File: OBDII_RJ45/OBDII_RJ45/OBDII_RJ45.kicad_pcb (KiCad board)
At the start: 2 copper layers, 19.7 x 22.2 mm, 2 parts, among them J1 Cantact, J2 Conn_01x02

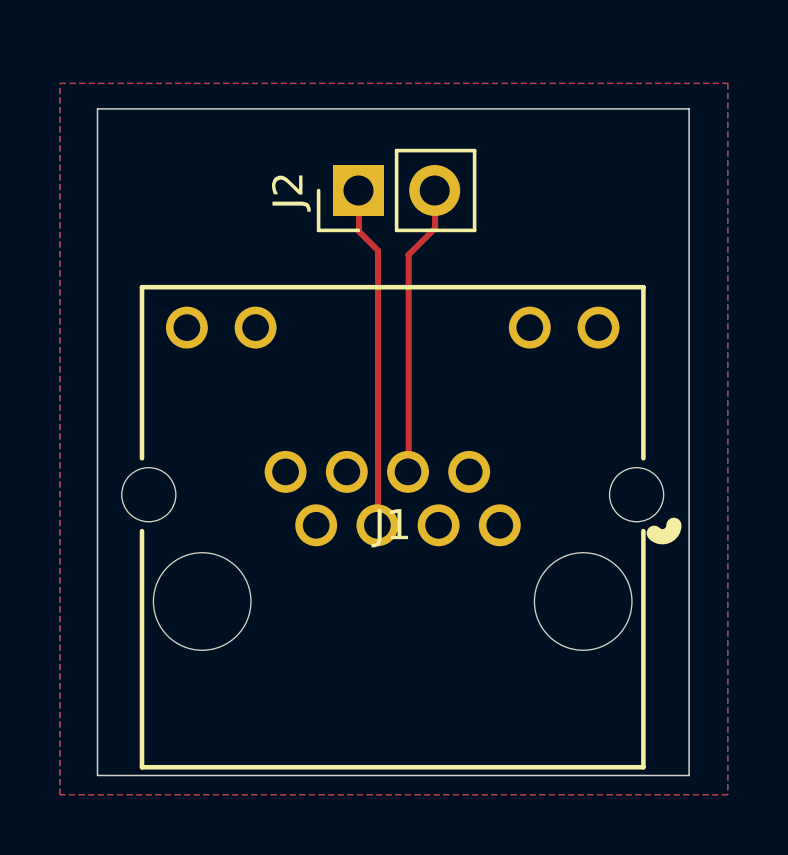
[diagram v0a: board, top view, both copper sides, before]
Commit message: feat: add GND between OBDII connector & OBDII_RJ45
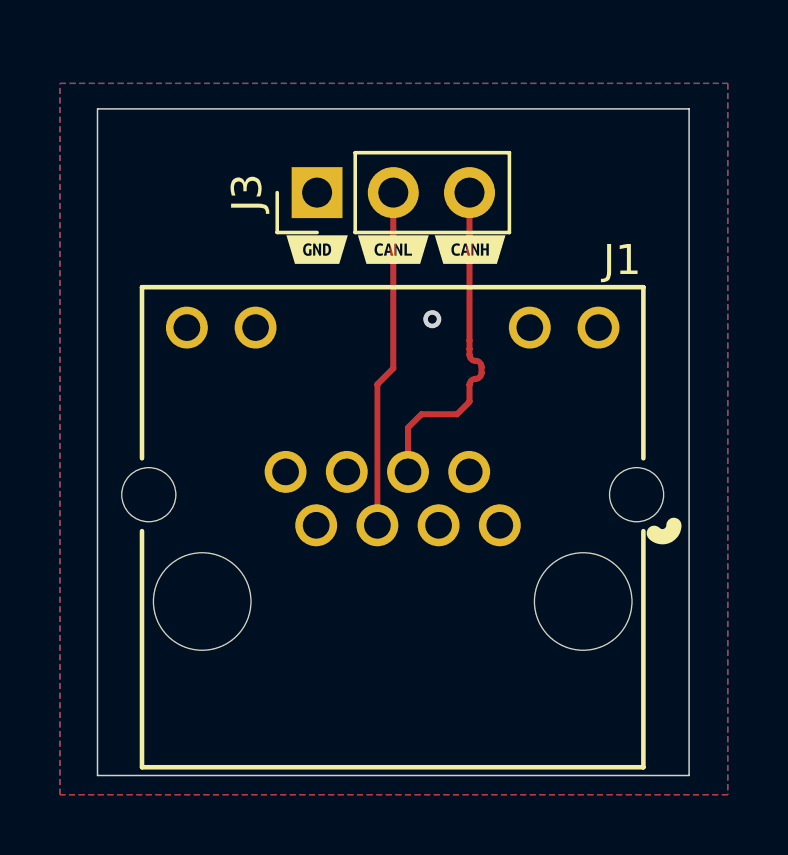
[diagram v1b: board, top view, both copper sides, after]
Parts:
- removed J2: Conn_01x02, Connector_PinHeader_2.54mm:PinHeader_1x02_P2.54mm_Vertical
- added J3: Conn_01x03, Connector_PinHeader_2.54mm:PinHeader_1x03_P2.54mm_Vertical, F.Cu at (22.3, 17.8)
- added kibuzzard-67DDB05E: G***, kibuzzard-67DDB05E, F.Cu at (27.4, 19.7)
- added kibuzzard-67DDB066: G***, kibuzzard-67DDB066, F.Cu at (24.9, 19.7)
- added kibuzzard-67DDB06D: G***, kibuzzard-67DDB06D, F.Cu at (22.3, 19.7)
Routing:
- net /CANH: track 9.76 -> 11.3 mm
- net GND: vias 0 -> 1

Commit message: feat(hw): add lcsc parts
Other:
- board size 19.7 x 22.2 mm -> 19.7 x 23.4 mm
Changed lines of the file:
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@@
 				(font
 					(size 0.001 0.001)
+					(thickness 0.15)
 				)
 			)
@@
 				(font
 					(size 0.001 0.001)
+					(thickness 0.15)
 				)
 			)
@@
 				(font
 					(size 0.001 0.001)
+					(thickness 0.15)
 				)
 			)
@@
 				(font
 					(size 0.001 0.001)
+					(thickness 0.15)
 				)
 			)
@@
 				(font
 					(size 0.001 0.001)
+					(thickness 0.15)
 				)
 			)
@@
 				(font
 					(size 0.001 0.001)
+					(thickness 0.15)
 				)
 			)
@@
 	)
 	(gr_rect
-		(start 15 15)
+		(start 15 13.79)
 		(end 34.72 37.22)
 		(stroke
@@
 		(polygon
 			(pts
-				(xy 13.75 14.15) (xy 36.01 14.15) (xy 36.01 37.86) (xy 13.75 37.86)
-			)
-		)
+				(xy 13.75 13.37) (xy 36.01 13.37) (xy 36.01 37.86) (xy 13.75 37.86)
+			)
+		)

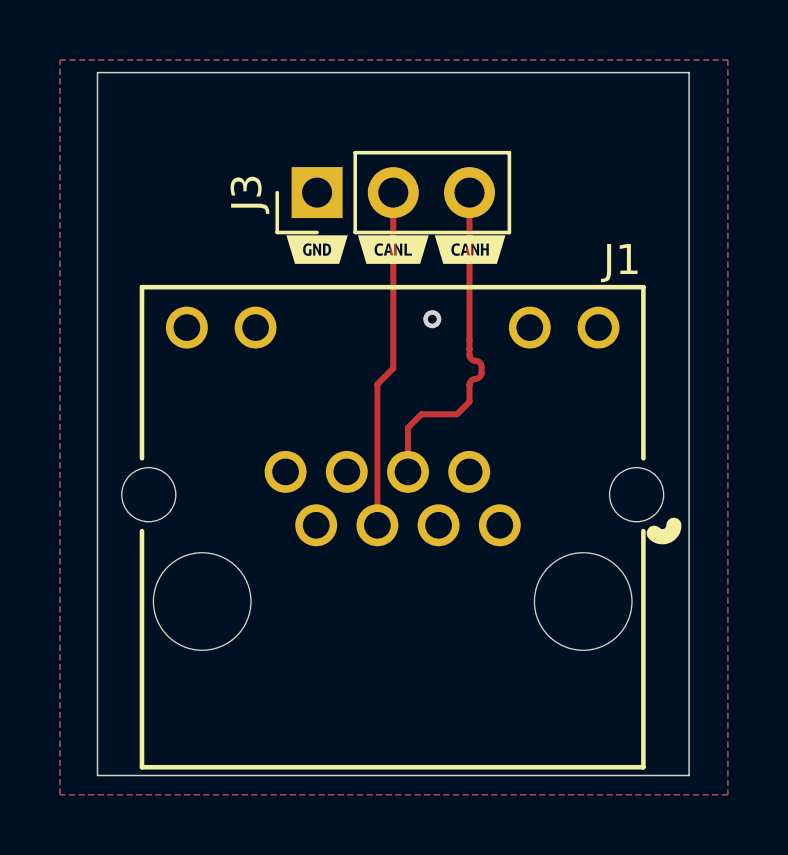
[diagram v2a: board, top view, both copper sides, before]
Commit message: feat(Hw):Update_Labels
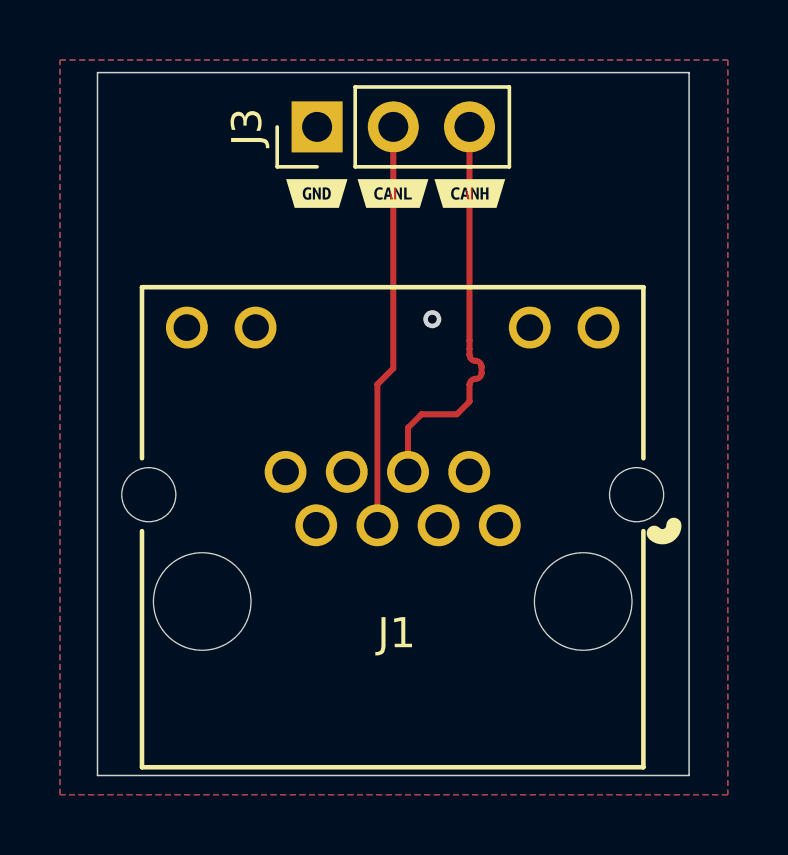
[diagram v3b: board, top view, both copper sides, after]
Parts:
- added G***: LOGO, Aesthetics:electronic_cats_logo_4x3, B.Cu at (24.9, 22.7)
- added kibuzzard-67FE8E6B: G***, kibuzzard-67FE8E6B, B.Cu at (24.9, 34.3)
- moved J3 2.19 mm to (22.3, 15.6)
- moved kibuzzard-67DDB05E 1.87 mm to (27.4, 17.8)
- moved kibuzzard-67DDB06D 1.87 mm to (22.3, 17.8)
- moved kibuzzard-67DDB066 1.87 mm to (24.9, 17.8)
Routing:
- net /CANH: track 11.3 -> 13.5 mm
- net /CANL: track 11.3 -> 13.5 mm

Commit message: Fix: CANbus routing for OBDII_RJ45
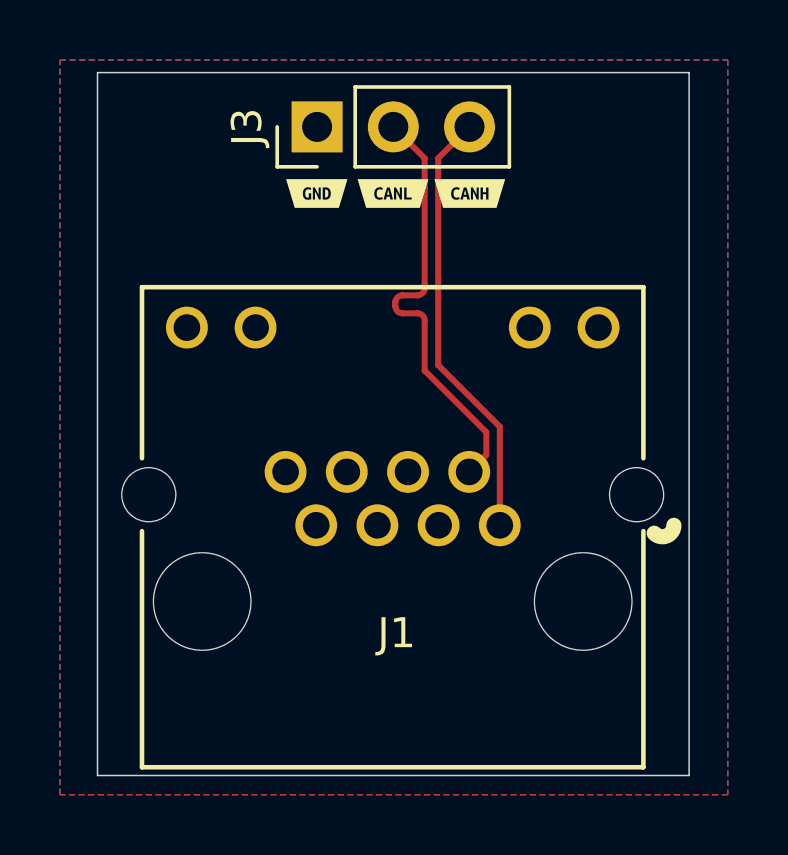
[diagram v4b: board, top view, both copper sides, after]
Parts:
- J1: value Cantact -> RJ45
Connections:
- J1 pad 1: unconnected-(J1-Pad1) -> /CAN+
- J1 pad 2: unconnected-(J1-Pad2) -> /CAN-
- J1 pad 3: unconnected-(J1-Pad3) -> GND
- J1 pad 4: /CANH -> unconnected-(J1-Pad4)
- J1 pad 5: /CANL -> unconnected-(J1-Pad5)
- J1 pad 7: GND -> unconnected-(J1-Pad7)
- J3 pad 2: /CANL -> /CAN-
- J3 pad 3: /CANH -> /CAN+
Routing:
- net /CAN+: track 0.00 -> 14.6 mm
- net /CAN-: track 0.00 -> 14.5 mm
- net /CANL: track 13.5 -> 0.00 mm
- net /CANH: track 13.5 -> 0.00 mm
- net GND: vias 1 -> 0
